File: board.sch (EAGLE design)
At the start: 32 parts

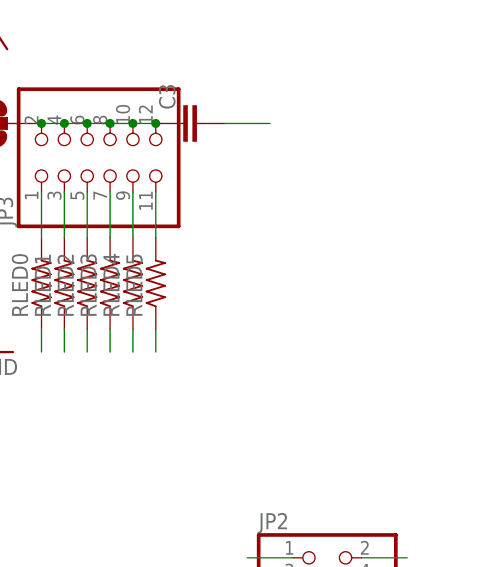
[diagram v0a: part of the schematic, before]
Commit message: routed, not very nice or optimal I guess, but it should work
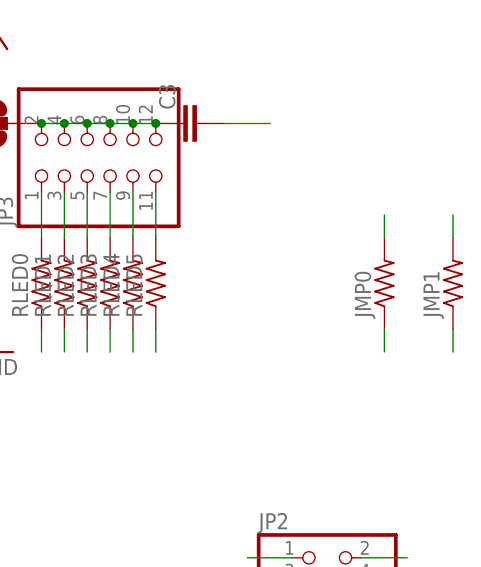
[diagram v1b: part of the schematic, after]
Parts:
- added JMP0, JMP1: (no value), resistor:R-US_R0805
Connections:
- net AGND: now also JMP0.1, JMP0.2, JMP1.1, JMP1.2
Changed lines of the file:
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@@
 <part name="+3.3V_VXMEGA" library="SparkFun-Passives" deviceset="SOLDERJUMPER" device="TRACE"/>
 <part name="C2" library="rcl" deviceset="C-EU" device="C0805K"/>
+<part name="JMP0" library="resistor" deviceset="R-US_" device="R0805"/>
+<part name="JMP1" library="resistor" deviceset="R-US_" device="R0805"/>
 </parts>
 <sheets>
@@
 </instance>
 <instance part="C2" gate="G$1" x="-22.86" y="76.2"/>
+<instance part="JMP0" gate="G$1" x="152.4" y="134.62" rot="R90"/>
+<instance part="JMP1" gate="G$1" x="160.02" y="134.62" rot="R90"/>
 </instances>
 <busses>
@@
 <pinref part="AGND_GND" gate="1" pin="1"/>
 </segment>
+<segment>
+<pinref part="JMP0" gate="G$1" pin="2"/>
+<wire x1="152.4" y1="139.7" x2="152.4" y2="142.24" width="0.1524" layer="91"/>
+</segment>
+<segment>
+<pinref part="JMP0" gate="G$1" pin="1"/>
+<wire x1="152.4" y1="129.54" x2="152.4" y2="127" width="0.1524" layer="91"/>
+</segment>
+<segment>
+<pinref part="JMP1" gate="G$1" pin="2"/>
+<wire x1="160.02" y1="139.7" x2="160.02" y2="142.24" width="0.1524" layer="91"/>
+</segment>
+<segment>
+<pinref part="JMP1" gate="G$1" pin="1"/>
+<wire x1="160.02" y1="129.54" x2="160.02" y2="127" width="0.1524" layer="91"/>
+</segment>
 </net>
 <net name="PA0" class="0">
@@
 </segment>
 </net>
-<net name="VLED" class="0">
+<net name="VLED" class="1">
 <segment>
 <wire x1="127" y1="152.4" x2="124.46" y2="152.4" width="0.1524" layer="91"/>

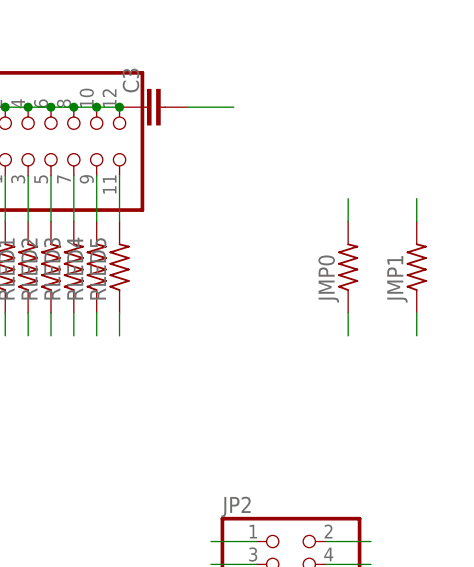
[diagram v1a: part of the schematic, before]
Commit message: mark the jumper resistor values
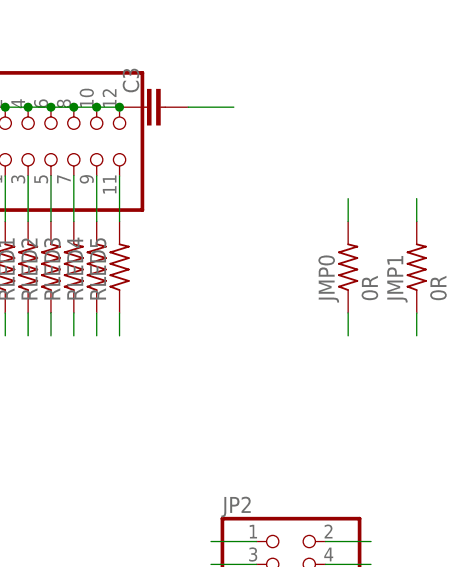
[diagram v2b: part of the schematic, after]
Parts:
- JMP0, JMP1: value (none) -> 0R
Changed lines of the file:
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@@
 <part name="+3.3V_VXMEGA" library="SparkFun-Passives" deviceset="SOLDERJUMPER" device="TRACE"/>
 <part name="C2" library="rcl" deviceset="C-EU" device="C0805K"/>
-<part name="JMP0" library="resistor" deviceset="R-US_" device="R0805"/>
-<part name="JMP1" library="resistor" deviceset="R-US_" device="R0805"/>
+<part name="JMP0" library="resistor" deviceset="R-US_" device="R0805" value="0R"/>
+<part name="JMP1" library="resistor" deviceset="R-US_" device="R0805" value="0R"/>
 </parts>
 <sheets>

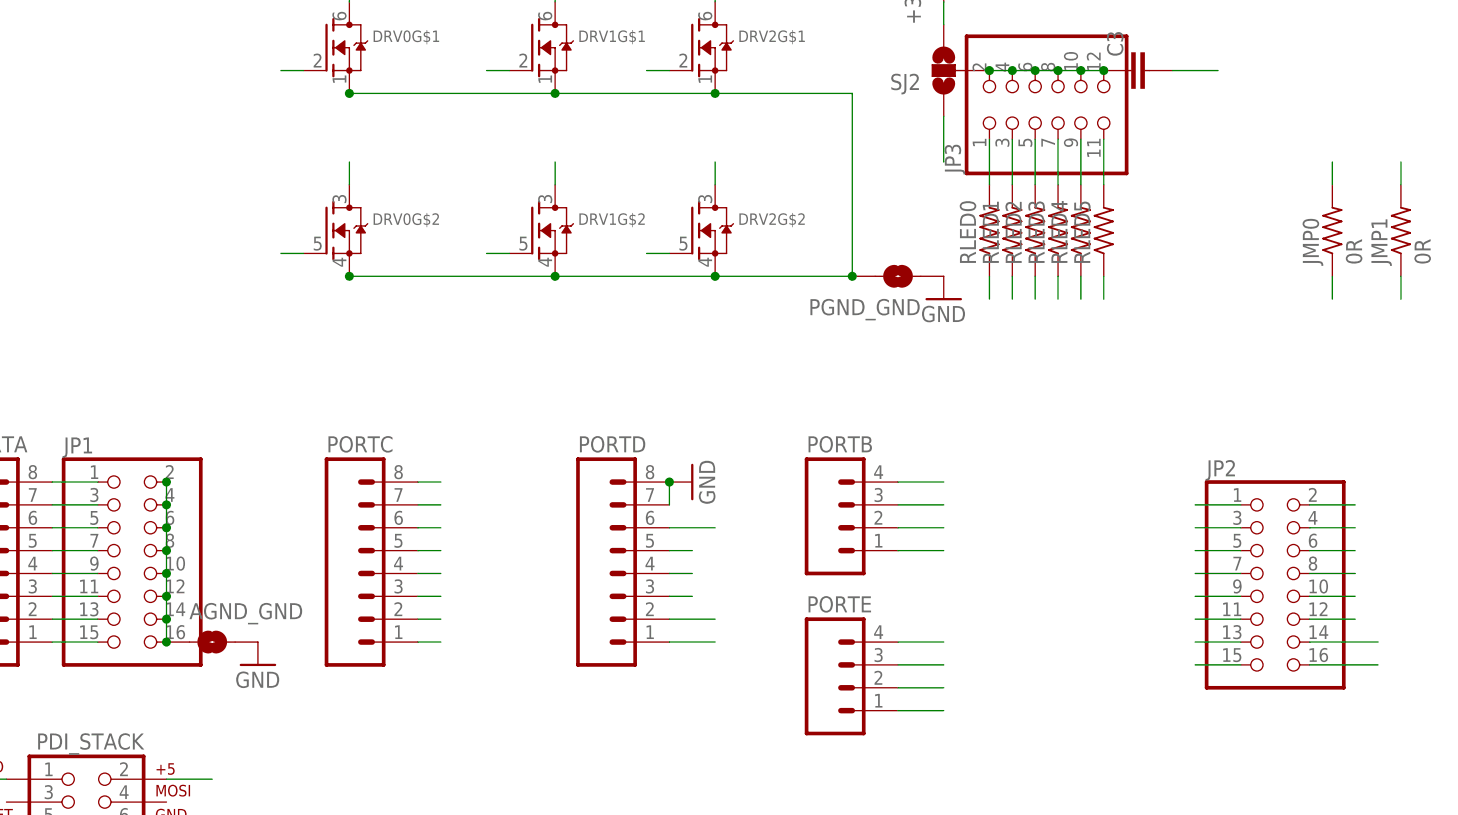
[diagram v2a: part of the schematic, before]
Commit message: get rid of agnd
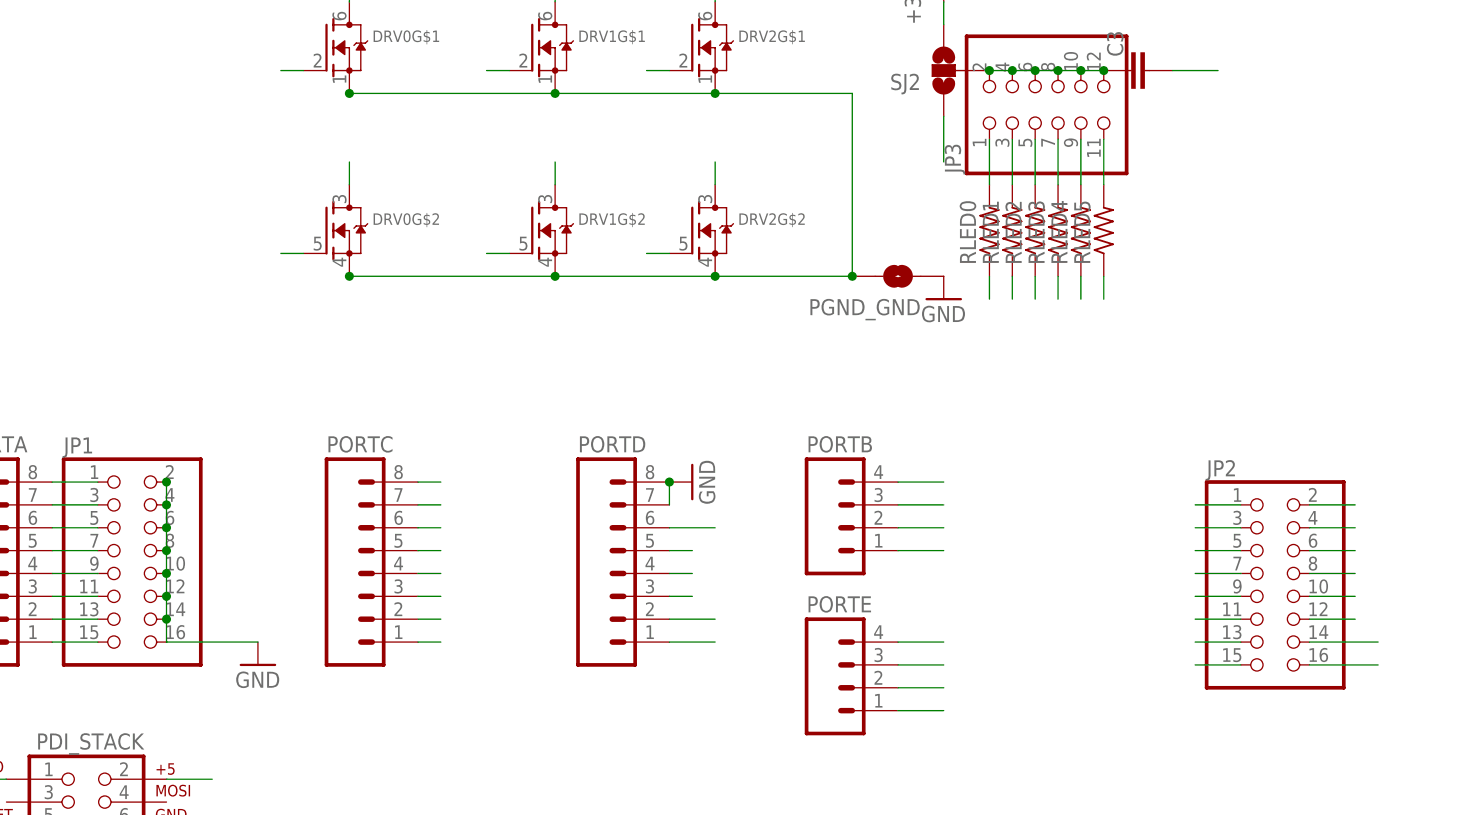
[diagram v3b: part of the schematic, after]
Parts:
- removed AGND_GND: SOLDERJUMPERTRACE, SparkFun-Passives:SOLDERJUMPERTRACE
- removed JMP0, JMP1: 0R, resistor:R-US_R0805
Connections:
- removed net AGND: AGND_GND.1, JMP0.1, JMP0.2, JMP1.1, JMP1.2, JP1.10, JP1.12, JP1.14, JP1.16, JP1.2, JP1.4, JP1.6, JP1.8
- net GND: now also JP1.10, JP1.12, JP1.14, JP1.16, JP1.2, JP1.4, JP1.6, JP1.8; no longer AGND_GND.2

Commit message: the xbee aref is not used on series2 anyway
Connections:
- net GND: now also XBEE.RES@14
- net PB0/XMEGA_AREF: no longer XBEE.RES@14
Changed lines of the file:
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@@
 <wire x1="33.02" y1="88.9" x2="22.86" y2="88.9" width="0.1524" layer="91"/>
+</segment>
+<segment>
+<pinref part="XBEE" gate="G$1" pin="RES@14"/>
+<wire x1="88.9" y1="40.64" x2="93.98" y2="40.64" width="0.1524" layer="91"/>
 </segment>
 </net>
@@
 </segment>
 <segment>
-<pinref part="XBEE" gate="G$1" pin="RES@14"/>
-<wire x1="88.9" y1="40.64" x2="93.98" y2="40.64" width="0.1524" layer="91"/>
-</segment>
-<segment>

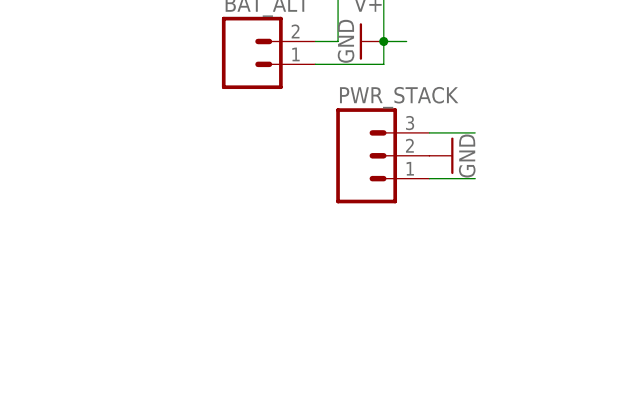
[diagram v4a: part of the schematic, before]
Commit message: placed lipo-charger second R that could be used to enable higher chg current via the UC
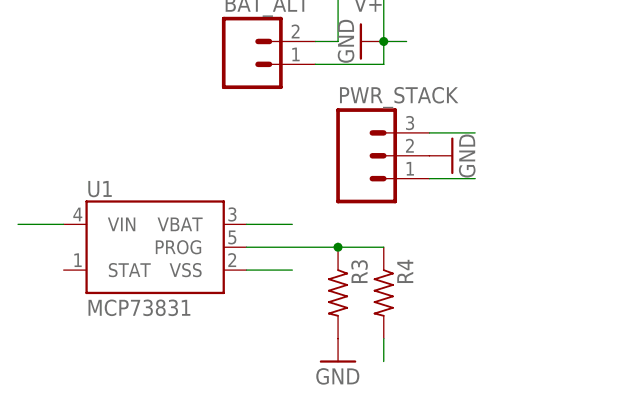
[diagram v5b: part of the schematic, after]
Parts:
- added R3, R4: (no value), rcl:R-US_R0603
- added U1: MCP73831, SparkFun-PowerIC:MCP73831
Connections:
- new net HIGHCCHG: R4.2
- new net RPROG: R3.1, R4.1, U1.PROG
- net GND: now also R3.2, U1.VSS
- net VBAT: now also U1.VBAT
- net VXMEGA_USB: now also U1.VIN
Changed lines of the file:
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@@
 <part name="+3.3V_VXMEGA" library="SparkFun-Passives" deviceset="SOLDERJUMPER" device="TRACE"/>
 <part name="C2" library="rcl" deviceset="C-EU" device="C0805K"/>
+<part name="U1" library="SparkFun-PowerIC" deviceset="MCP73831" device=""/>
+<part name="R3" library="rcl" deviceset="R-US_" device="R0603"/>
+<part name="R4" library="rcl" deviceset="R-US_" device="R0603"/>
+<part name="GND10" library="supply1" deviceset="GND" device=""/>
 </parts>
 <sheets>
@@
 </instance>
 <instance part="C2" gate="G$1" x="-22.86" y="76.2"/>
+<instance part="U1" gate="G$1" x="-25.4" y="25.4"/>
+<instance part="R3" gate="G$1" x="-5.08" y="20.32" rot="R270"/>
+<instance part="R4" gate="G$1" x="0" y="20.32" rot="R270"/>
+<instance part="GND10" gate="1" x="-5.08" y="12.7"/>
 </instances>
 <busses>
@@
 <wire x1="88.9" y1="40.64" x2="93.98" y2="40.64" width="0.1524" layer="91"/>
 </segment>
+<segment>
+<pinref part="U1" gate="G$1" pin="VSS"/>
+<wire x1="-15.24" y1="22.86" x2="-10.16" y2="22.86" width="0.1524" layer="91"/>
+</segment>
+<segment>
+<pinref part="R3" gate="G$1" pin="2"/>
+<pinref part="GND10" gate="1" pin="GND"/>
+</segment>
 </net>
 <net name="VBAT" class="1">
@@
 <pinref part="SJ2" gate="G$1" pin="1"/>
 </segment>
+<segment>
+<pinref part="U1" gate="G$1" pin="VBAT"/>
+<wire x1="-15.24" y1="27.94" x2="-10.16" y2="27.94" width="0.1524" layer="91"/>
+</segment>
 </net>
 <net name="PDI_DATA" class="0">
@@
 <pinref part="PWR_STACK" gate="G$1" pin="1"/>
 <wire x1="5.08" y1="33.02" x2="10.16" y2="33.02" width="0.1524" layer="91"/>
+</segment>
+<segment>
+<pinref part="U1" gate="G$1" pin="VIN"/>
+<wire x1="-35.56" y1="27.94" x2="-40.64" y2="27.94" width="0.1524" layer="91"/>
 </segment>
 </net>
@@
 </segment>
 </net>
+<net name="RPROG" class="0">
+<segment>
+<pinref part="U1" gate="G$1" pin="PROG"/>
+<pinref part="R3" gate="G$1" pin="1"/>
+<wire x1="-15.24" y1="25.4" x2="-5.08" y2="25.4" width="0.1524" layer="91"/>
+<pinref part="R4" gate="G$1" pin="1"/>
+<wire x1="-5.08" y1="25.4" x2="0" y2="25.4" width="0.1524" layer="91"/>
+<junction x="-5.08" y="25.4"/>
+</segment>
+</net>
+<net name="HIGHCCHG" class="0">
+<segment>
+<pinref part="R4" gate="G$1" pin="2"/>
+<wire x1="0" y1="15.24" x2="0" y2="12.7" width="0.1524" layer="91"/>
+</segment>
+</net>

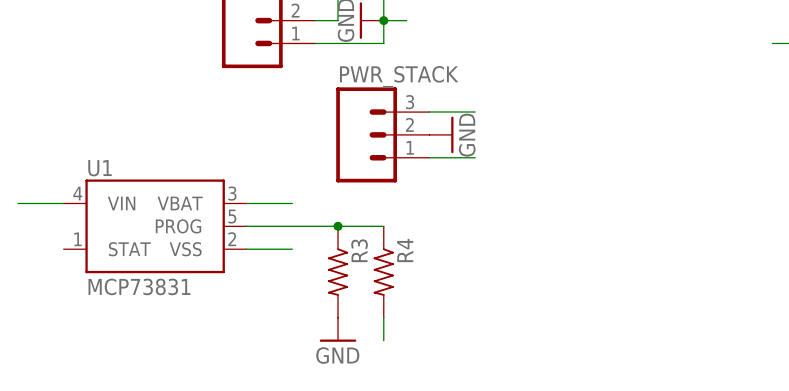
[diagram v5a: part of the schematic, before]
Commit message: 100mA charge current normally, sink PD5 to GND to make it 500mA
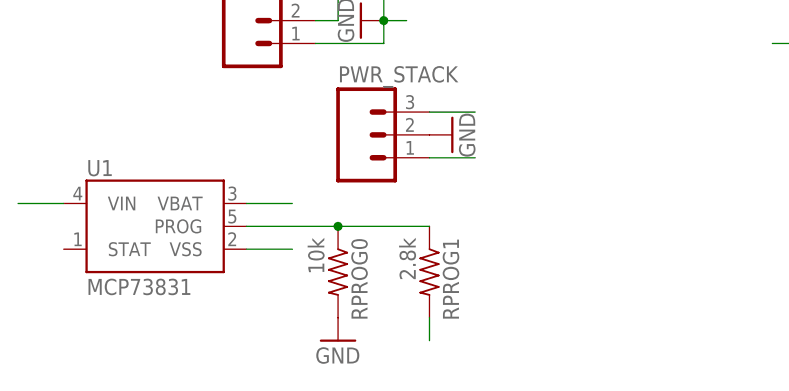
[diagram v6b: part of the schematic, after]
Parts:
- removed R4: (no value), rcl:R-US_R0603
- added RPROG1: 2.8k, rcl:R-US_R0603
- RPROG0: value (none) -> 10k
- renumbered R3 to RPROG0
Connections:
- removed net HIGHCCHG: R4.2
- removed net PD5: JP2.15, PORTD.6
- new net PD5/CHGCTRL: JP2.15, PORTD.6, RPROG1.2
- net RPROG: now also RPROG1.1; no longer R4.1
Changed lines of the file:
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@@
 <part name="C2" library="rcl" deviceset="C-EU" device="C0805K"/>
 <part name="U1" library="SparkFun-PowerIC" deviceset="MCP73831" device=""/>
-<part name="R3" library="rcl" deviceset="R-US_" device="R0603"/>
-<part name="R4" library="rcl" deviceset="R-US_" device="R0603"/>
+<part name="RPROG0" library="rcl" deviceset="R-US_" device="R0603" value="10k"/>
+<part name="RPROG1" library="rcl" deviceset="R-US_" device="R0603" value="2.8k"/>
 <part name="GND10" library="supply1" deviceset="GND" device=""/>
 </parts>
@@
 <instance part="C2" gate="G$1" x="-22.86" y="76.2"/>
 <instance part="U1" gate="G$1" x="-25.4" y="25.4"/>
-<instance part="R3" gate="G$1" x="-5.08" y="20.32" rot="R270"/>
-<instance part="R4" gate="G$1" x="0" y="20.32" rot="R270"/>
+<instance part="RPROG0" gate="G$1" x="-5.08" y="20.32" rot="R270"/>
+<instance part="RPROG1" gate="G$1" x="5.08" y="20.32" rot="R270"/>
 <instance part="GND10" gate="1" x="-5.08" y="12.7"/>
 </instances>
@@
 </segment>
 <segment>
-<pinref part="R3" gate="G$1" pin="2"/>
+<pinref part="RPROG0" gate="G$1" pin="2"/>
 <pinref part="GND10" gate="1" pin="GND"/>
 </segment>
@@
 </segment>
 </net>
-<net name="VXMEGA_USB" class="0">
+<net name="VXMEGA_USB" class="1">
 <segment>
 <pinref part="PWR_STACK" gate="G$1" pin="1"/>
@@
 </segment>
 </net>
-<net name="PD5" class="0">
+<net name="PD5/CHGCTRL" class="0">
 <segment>
 <pinref part="PORTD" gate="G$1" pin="6"/>
@@
 <wire x1="142.24" y1="86.36" x2="137.16" y2="86.36" width="0.1524" layer="91"/>
 </segment>
+<segment>
+<pinref part="RPROG1" gate="G$1" pin="2"/>
+<wire x1="5.08" y1="15.24" x2="5.08" y2="12.7" width="0.1524" layer="91"/>
+</segment>
 </net>
 <net name="RPROG" class="0">
 <segment>
 <pinref part="U1" gate="G$1" pin="PROG"/>
-<pinref part="R3" gate="G$1" pin="1"/>
+<pinref part="RPROG0" gate="G$1" pin="1"/>
 <wire x1="-15.24" y1="25.4" x2="-5.08" y2="25.4" width="0.1524" layer="91"/>
-<pinref part="R4" gate="G$1" pin="1"/>
-<wire x1="-5.08" y1="25.4" x2="0" y2="25.4" width="0.1524" layer="91"/>
+<pinref part="RPROG1" gate="G$1" pin="1"/>
+<wire x1="-5.08" y1="25.4" x2="5.08" y2="25.4" width="0.1524" layer="91"/>
 <junction x="-5.08" y="25.4"/>
 </segment>
 </net>
-<net name="HIGHCCHG" class="0">
-<segment>
-<pinref part="R4" gate="G$1" pin="2"/>
-<wire x1="0" y1="15.24" x2="0" y2="12.7" width="0.1524" layer="91"/>
-</segment>
-</net>
